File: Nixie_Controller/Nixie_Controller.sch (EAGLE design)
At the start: 59 parts, among them IC1 4028N, T1 MMBTA42, T10 MMBTA42, T11 MMBTA42, T12 MMBTA42, T13 MMBTA42, T14 MMBTA42, T2 MMBTA42, T3 MMBTA42, T4 MMBTA42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

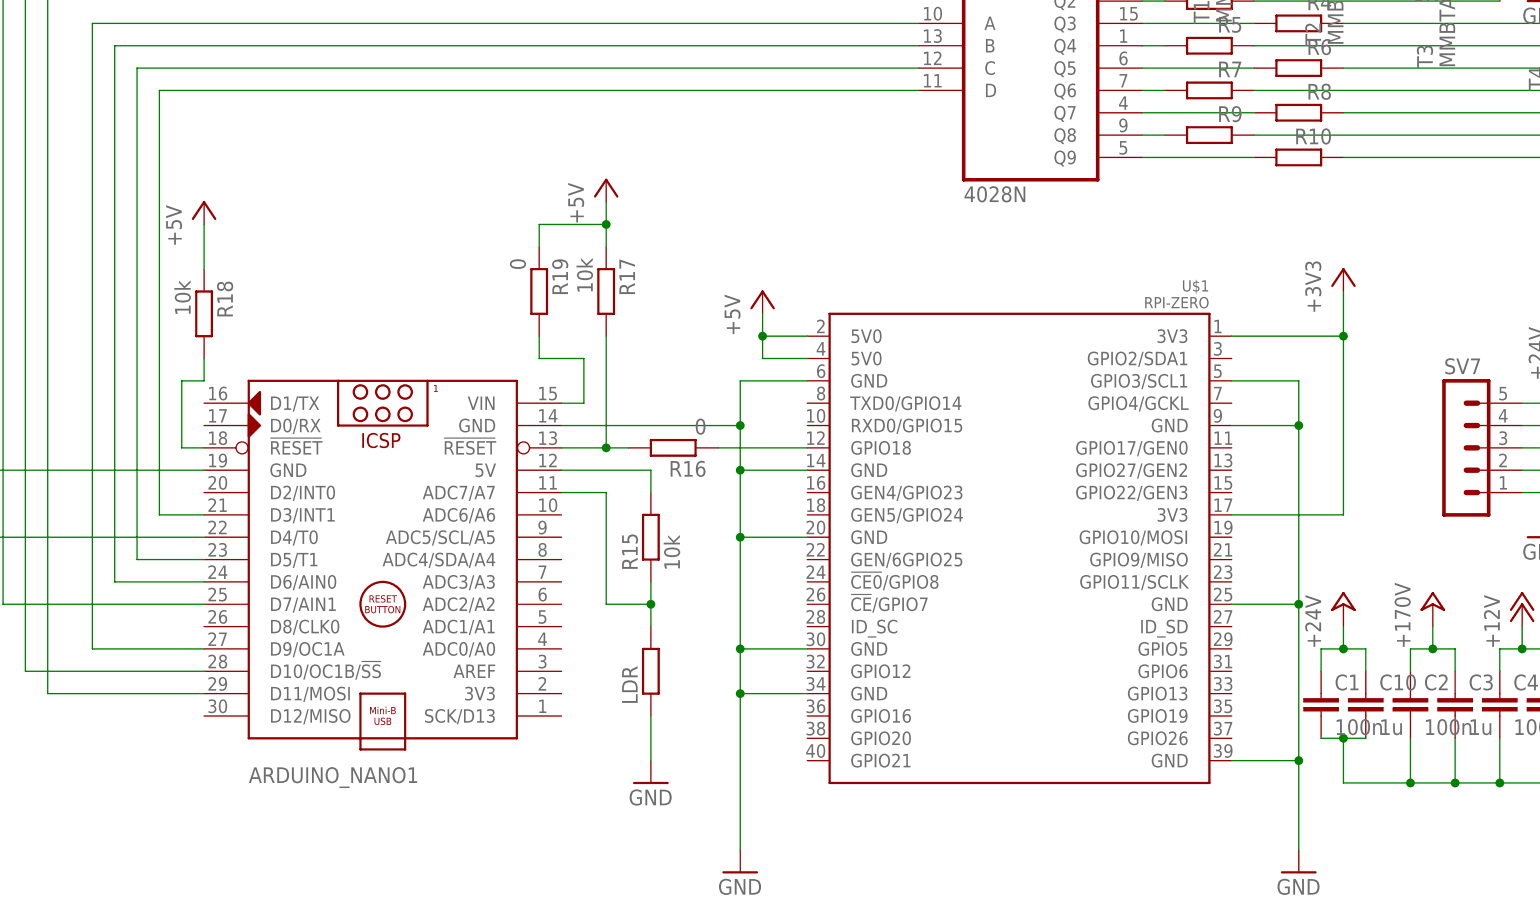
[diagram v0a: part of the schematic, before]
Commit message: fix: add zero ohms to supplies
Add a zero ohm resistor between the Arduino 3.3V and the 3.3V supply voltage.
Add a zero ohm resistor between the raspberry pi 5V and 3.3V and their respective supply voltages.
Remove the second connection to the arduino reset, because they are internally connected
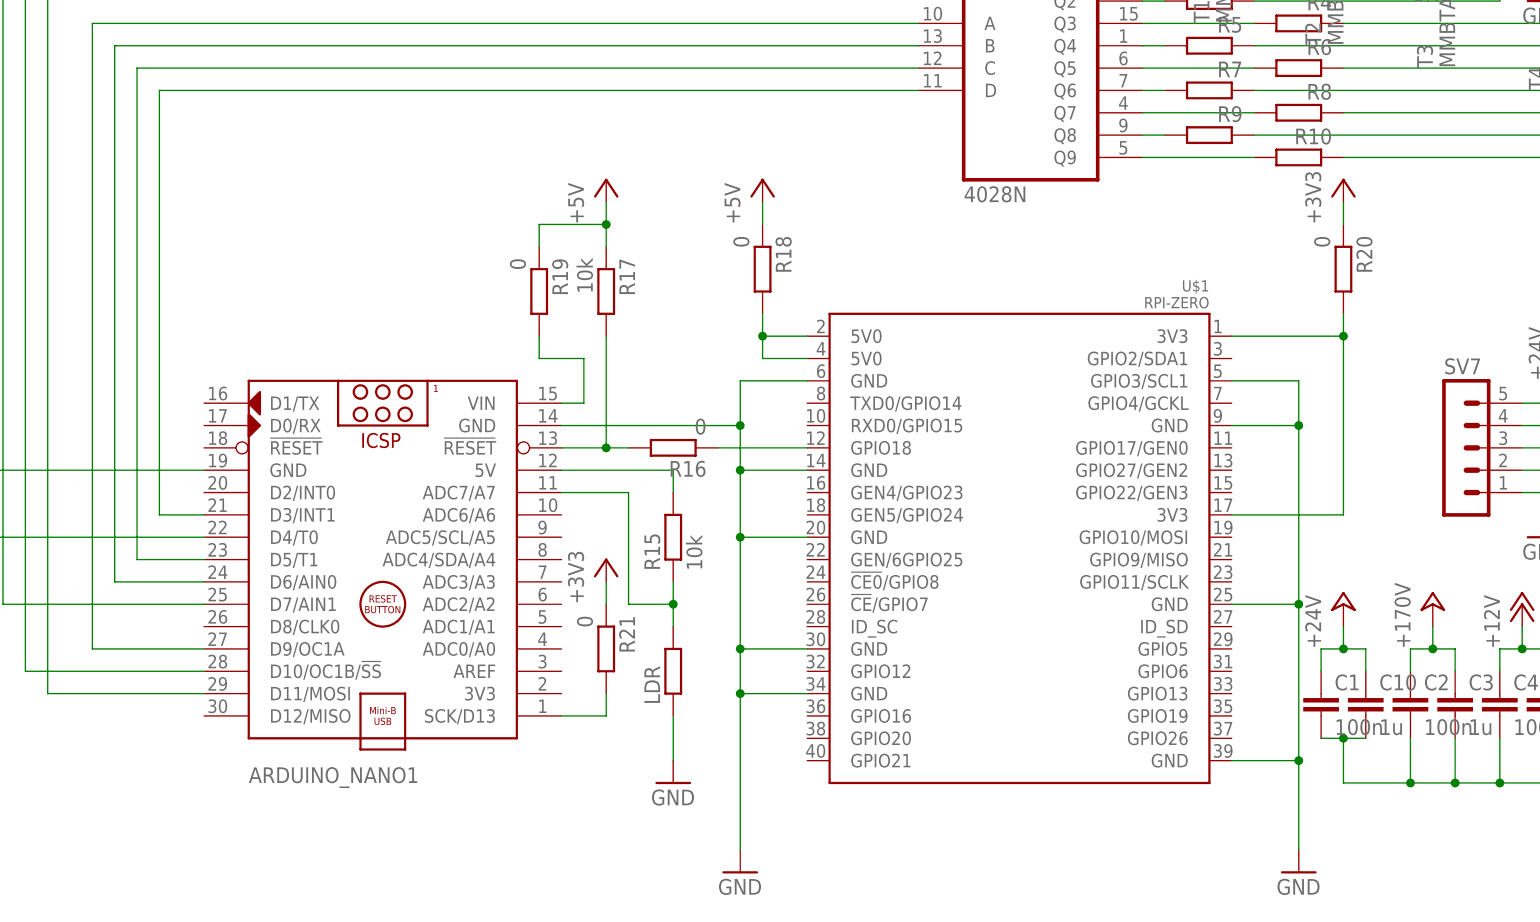
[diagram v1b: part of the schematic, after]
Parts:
- added R20, R21: 0, resistor:R-EU_R0603
- R18: value 10k -> 0
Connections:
- removed net N$95: ARDUINO_NANO1.!RESET@1, R18.2
- new net 3V3@2: R20.2, U$1.3V3@1, U$1.3V3@2
- new net N$39: ARDUINO_NANO1.SCK/D13, R21.2
- net +3V3: now also R20.1, R21.1; no longer U$1.3V3@1, U$1.3V3@2
- net VDD: now also R18.2
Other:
- moved on the sheet: LDR, R15, R18
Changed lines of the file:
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@@
 <part name="R16" library="resistor" deviceset="R-EU_" device="R0603" value="0"/>
 <part name="R17" library="resistor" deviceset="R-EU_" device="R0603" value="10k"/>
-<part name="R18" library="resistor" deviceset="R-EU_" device="R0603" value="10k"/>
-<part name="P+17" library="supply1" deviceset="+5V" device=""/>
 <part name="P+18" library="supply1" deviceset="+5V" device=""/>
 <part name="R19" library="resistor" deviceset="R-EU_" device="R0603" value="0"/>
 <part name="GND19" library="supply1" deviceset="GND" device=""/>
 <part name="GND20" library="supply1" deviceset="GND" device=""/>
+<part name="+3V5" library="supply1" deviceset="+3V3" device=""/>
+<part name="R18" library="resistor" deviceset="R-EU_" device="R0603" value="0"/>
+<part name="R20" library="resistor" deviceset="R-EU_" device="R0603" value="0"/>
+<part name="R21" library="resistor" deviceset="R-EU_" device="R0603" value="0"/>
 </parts>
 <sheets>
@@
 <instance part="SV4" gate="1" x="180.34" y="292.1" rot="MR0"/>
 <instance part="SV2" gate="1" x="180.34" y="236.22" rot="MR0"/>
-<instance part="+3V1" gate="G$1" x="109.22" y="170.18"/>
+<instance part="+3V1" gate="G$1" x="109.22" y="180.34"/>
 <instance part="P+8" gate="1" x="243.84" y="160.02"/>
 <instance part="GND44" gate="1" x="104.14" y="101.6"/>
@@
 <instance part="R12" gate="G$1" x="215.9" y="332.74" rot="R90"/>
 <instance part="R11" gate="G$1" x="223.52" y="320.04" rot="R90"/>
-<instance part="LDR" gate="G$1" x="30.48" y="124.46" rot="R90"/>
-<instance part="R15" gate="G$1" x="30.48" y="139.7" rot="R90"/>
+<instance part="LDR" gate="G$1" x="33.02" y="124.46" rot="R90"/>
+<instance part="R15" gate="G$1" x="33.02" y="139.7" rot="R90"/>
 <instance part="T1" gate="G$1" x="101.6" y="208.28" rot="R90"/>
 <instance part="T2" gate="G$1" x="114.3" y="205.74" rot="R90"/>
@@
 <instance part="ARDUINO_NANO1" gate="G$1" x="0" y="132.08"/>
 <instance part="GND16" gate="1" x="-48.26" y="111.76"/>
-<instance part="GND17" gate="1" x="30.48" y="111.76"/>
-<instance part="P+7" gate="1" x="43.18" y="167.64"/>
+<instance part="GND17" gate="1" x="33.02" y="111.76"/>
+<instance part="P+7" gate="1" x="43.18" y="180.34"/>
 <instance part="U$1" gate="G$1" x="73.66" y="132.08" rot="MR0"/>
 <instance part="SV6" gate="G$1" x="165.1" y="147.32"/>
@@
 <instance part="R16" gate="G$1" x="33.02" y="149.86" rot="R180"/>
 <instance part="R17" gate="G$1" x="25.4" y="167.64" rot="R270"/>
-<instance part="R18" gate="G$1" x="-20.32" y="165.1" rot="R270"/>
-<instance part="P+17" gate="1" x="-20.32" y="177.8"/>
 <instance part="P+18" gate="1" x="25.4" y="180.34"/>
 <instance part="R19" gate="G$1" x="17.78" y="167.64" rot="R270"/>
 <instance part="GND19" gate="1" x="317.5" y="200.66"/>
 <instance part="GND20" gate="1" x="317.5" y="109.22"/>
+<instance part="+3V5" gate="G$1" x="25.4" y="137.16"/>
+<instance part="R18" gate="G$1" x="43.18" y="170.18" rot="R270"/>
+<instance part="R20" gate="G$1" x="109.22" y="170.18" rot="R270"/>
+<instance part="R21" gate="G$1" x="25.4" y="127" rot="R270"/>
 </instances>
 <busses>
@@
 <pinref part="LDR" gate="G$1" pin="1"/>
 <pinref part="GND17" gate="1" pin="GND"/>
-<wire x1="30.48" y1="114.3" x2="30.48" y2="119.38" width="0.1524" layer="91"/>
+<wire x1="33.02" y1="114.3" x2="33.02" y2="119.38" width="0.1524" layer="91"/>
 </segment>
 <segment>
@@
 <net name="+3V3" class="0">
 <segment>
-<pinref part="+3V1" gate="G$1" pin="+3V3"/>
-<wire x1="109.22" y1="167.64" x2="109.22" y2="162.56" width="0.1524" layer="91"/>
-<wire x1="109.22" y1="162.56" x2="109.22" y2="142.24" width="0.1524" layer="91"/>
-<wire x1="96.52" y1="162.56" x2="109.22" y2="162.56" width="0.1524" layer="91"/>
-<junction x="109.22" y="162.56"/>
-<wire x1="109.22" y1="142.24" x2="96.52" y2="142.24" width="0.1524" layer="91"/>
-<pinref part="U$1" gate="G$1" pin="3V3@1"/>
-<pinref part="U$1" gate="G$1" pin="3V3@2"/>
-</segment>
-<segment>
 <pinref part="SV7" gate="G$1" pin="2"/>
 <pinref part="+3V2" gate="G$1" pin="+3V3"/>
@@
 <wire x1="172.72" y1="144.78" x2="200.66" y2="144.78" width="0.1524" layer="91"/>
 <wire x1="200.66" y1="144.78" x2="200.66" y2="157.48" width="0.1524" layer="91"/>
+</segment>
+<segment>
+<pinref part="+3V5" gate="G$1" pin="+3V3"/>
+<pinref part="R21" gate="G$1" pin="1"/>
+<wire x1="25.4" y1="134.62" x2="25.4" y2="132.08" width="0.1524" layer="91"/>
+</segment>
+<segment>
+<pinref part="+3V1" gate="G$1" pin="+3V3"/>
+<pinref part="R20" gate="G$1" pin="1"/>
+<wire x1="109.22" y1="177.8" x2="109.22" y2="175.26" width="0.1524" layer="91"/>
 </segment>
 </net>
@@
 </segment>
 <segment>
-<pinref part="P+7" gate="1" pin="+5V"/>
 <wire x1="48.26" y1="160.02" x2="43.18" y2="160.02" width="0.1524" layer="91"/>
 <wire x1="43.18" y1="160.02" x2="43.18" y2="162.56" width="0.1524" layer="91"/>
-<wire x1="43.18" y1="165.1" x2="43.18" y2="162.56" width="0.1524" layer="91"/>
 <wire x1="43.18" y1="162.56" x2="48.26" y2="162.56" width="0.1524" layer="91"/>
-<junction x="43.18" y="162.56"/>
 <pinref part="U$1" gate="G$1" pin="5V0@1"/>
 <pinref part="U$1" gate="G$1" pin="5V0@2"/>
+<pinref part="R18" gate="G$1" pin="2"/>
+<wire x1="43.18" y1="165.1" x2="43.18" y2="162.56" width="0.1524" layer="91"/>
+<junction x="43.18" y="162.56"/>
 </segment>
 <segment>
@@
 <pinref part="ARDUINO_NANO1" gate="G$1" pin="5V"/>
 <pinref part="R15" gate="G$1" pin="2"/>
-<wire x1="20.32" y1="147.32" x2="30.48" y2="147.32" width="0.1524" layer="91"/>
-<wire x1="30.48" y1="147.32" x2="30.48" y2="144.78" width="0.1524" layer="91"/>
+<wire x1="20.32" y1="147.32" x2="33.02" y2="147.32" width="0.1524" layer="91"/>
+<wire x1="33.02" y1="147.32" x2="33.02" y2="144.78" width="0.1524" layer="91"/>
 </segment>
 </net>
@@
 <pinref part="R15" gate="G$1" pin="1"/>
 <pinref part="LDR" gate="G$1" pin="2"/>
-<wire x1="30.48" y1="134.62" x2="30.48" y2="132.08" width="0.1524" layer="91"/>
-<wire x1="30.48" y1="132.08" x2="30.48" y2="129.54" width="0.1524" layer="91"/>
-<wire x1="30.48" y1="132.08" x2="25.4" y2="132.08" width="0.1524" layer="91"/>
-<wire x1="25.4" y1="132.08" x2="25.4" y2="144.78" width="0.1524" layer="91"/>
+<wire x1="33.02" y1="134.62" x2="33.02" y2="132.08" width="0.1524" layer="91"/>
+<wire x1="33.02" y1="132.08" x2="33.02" y2="129.54" width="0.1524" layer="91"/>
+<wire x1="33.02" y1="132.08" x2="27.94" y2="132.08" width="0.1524" layer="91"/>
+<wire x1="27.94" y1="132.08" x2="27.94" y2="144.78" width="0.1524" layer="91"/>
 <pinref part="ARDUINO_NANO1" gate="G$1" pin="ADC7/A7"/>
-<wire x1="25.4" y1="144.78" x2="20.32" y2="144.78" width="0.1524" layer="91"/>
-<junction x="30.48" y="132.08"/>
+<wire x1="27.94" y1="144.78" x2="20.32" y2="144.78" width="0.1524" layer="91"/>
+<junction x="33.02" y="132.08"/>
 </segment>
 </net>
@@
 </segment>
 </net>
-<net name="N$95" class="0">
-<segment>
-<pinref part="ARDUINO_NANO1" gate="G$1" pin="!RESET@1"/>
-<wire x1="-20.32" y1="149.86" x2="-22.86" y2="149.86" width="0.1524" layer="91"/>
-<wire x1="-22.86" y1="149.86" x2="-22.86" y2="157.48" width="0.1524" layer="91"/>
-<wire x1="-22.86" y1="157.48" x2="-20.32" y2="157.48" width="0.1524" layer="91"/>
-<pinref part="R18" gate="G$1" pin="2"/>
-<wire x1="-20.32" y1="157.48" x2="-20.32" y2="160.02" width="0.1524" layer="91"/>
-</segment>
-</net>
 <net name="+5V" class="0">
 <segment>
@@
 </segment>
 <segment>
+<pinref part="P+7" gate="1" pin="+5V"/>
 <pinref part="R18" gate="G$1" pin="1"/>
-<pinref part="P+17" gate="1" pin="+5V"/>
-<wire x1="-20.32" y1="175.26" x2="-20.32" y2="170.18" width="0.1524" layer="91"/>
+<wire x1="43.18" y1="177.8" x2="43.18" y2="175.26" width="0.1524" layer="91"/>
 </segment>
 </net>
@@
 </segment>
 </net>
+<net name="N$39" class="0">
+<segment>
+<pinref part="ARDUINO_NANO1" gate="G$1" pin="SCK/D13"/>
+<pinref part="R21" gate="G$1" pin="2"/>
+<wire x1="20.32" y1="119.38" x2="25.4" y2="119.38" width="0.1524" layer="91"/>
+<wire x1="25.4" y1="119.38" x2="25.4" y2="121.92" width="0.1524" layer="91"/>
+</segment>
+</net>
+<net name="3V3@2" class="0">
+<segment>
+<wire x1="109.22" y1="162.56" x2="109.22" y2="142.24" width="0.1524" layer="91"/>
+<wire x1="96.52" y1="162.56" x2="109.22" y2="162.56" width="0.1524" layer="91"/>
+<wire x1="109.22" y1="142.24" x2="96.52" y2="142.24" width="0.1524" layer="91"/>
+<pinref part="U$1" gate="G$1" pin="3V3@1"/>
+<pinref part="U$1" gate="G$1" pin="3V3@2"/>
+<pinref part="R20" gate="G$1" pin="2"/>
+<wire x1="109.22" y1="162.56" x2="109.22" y2="165.1" width="0.1524" layer="91"/>
+<junction x="109.22" y="162.56"/>
+</segment>
+</net>

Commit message: fix: add resistors from schematic fix
Add the three 0 ohm resistors to the board, which were added in the schematic fix
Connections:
- net +5V: now also R18.2, U$1.5V0@1, U$1.5V0@2; no longer R17.1, R18.1, R19.1
- net VDD: now also R17.1, R18.1, R19.1; no longer R18.2, U$1.5V0@1, U$1.5V0@2
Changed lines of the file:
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@@
-</segment>
-<segment>
-<wire x1="48.26" y1="160.02" x2="43.18" y2="160.02" width="0.1524" layer="91"/>
-<wire x1="43.18" y1="160.02" x2="43.18" y2="162.56" width="0.1524" layer="91"/>
-<wire x1="43.18" y1="162.56" x2="48.26" y2="162.56" width="0.1524" layer="91"/>
-<pinref part="U$1" gate="G$1" pin="5V0@1"/>
-<pinref part="U$1" gate="G$1" pin="5V0@2"/>
-<pinref part="R18" gate="G$1" pin="2"/>
-<wire x1="43.18" y1="165.1" x2="43.18" y2="162.56" width="0.1524" layer="91"/>
-<junction x="43.18" y="162.56"/>
 </segment>
 <segment>
@@
 <wire x1="236.22" y1="208.28" x2="238.76" y2="208.28" width="0.1524" layer="91"/>
 <wire x1="238.76" y1="208.28" x2="238.76" y2="220.98" width="0.1524" layer="91"/>
+</segment>
+<segment>
+<pinref part="R17" gate="G$1" pin="1"/>
+<pinref part="P+18" gate="1" pin="+5V"/>
+<wire x1="25.4" y1="177.8" x2="25.4" y2="175.26" width="0.1524" layer="91"/>
+<pinref part="R19" gate="G$1" pin="1"/>
+<wire x1="25.4" y1="175.26" x2="25.4" y2="172.72" width="0.1524" layer="91"/>
+<wire x1="17.78" y1="172.72" x2="17.78" y2="175.26" width="0.1524" layer="91"/>
+<wire x1="17.78" y1="175.26" x2="25.4" y2="175.26" width="0.1524" layer="91"/>
+<junction x="25.4" y="175.26"/>
+</segment>
+<segment>
+<pinref part="P+7" gate="1" pin="+5V"/>
+<pinref part="R18" gate="G$1" pin="1"/>
+<wire x1="43.18" y1="177.8" x2="43.18" y2="175.26" width="0.1524" layer="91"/>
 </segment>
 </net>
@@
 </segment>
 </net>
-<net name="+5V" class="0">
-<segment>
-<pinref part="R17" gate="G$1" pin="1"/>
-<pinref part="P+18" gate="1" pin="+5V"/>
-<wire x1="25.4" y1="177.8" x2="25.4" y2="175.26" width="0.1524" layer="91"/>
-<pinref part="R19" gate="G$1" pin="1"/>
-<wire x1="25.4" y1="175.26" x2="25.4" y2="172.72" width="0.1524" layer="91"/>
-<wire x1="17.78" y1="172.72" x2="17.78" y2="175.26" width="0.1524" layer="91"/>
-<wire x1="17.78" y1="175.26" x2="25.4" y2="175.26" width="0.1524" layer="91"/>
-<junction x="25.4" y="175.26"/>
-</segment>
-<segment>
-<pinref part="P+7" gate="1" pin="+5V"/>
-<pinref part="R18" gate="G$1" pin="1"/>
-<wire x1="43.18" y1="177.8" x2="43.18" y2="175.26" width="0.1524" layer="91"/>
-</segment>
-</net>
 <net name="N$96" class="0">
 <segment>
@@
 </segment>
 </net>
+<net name="+5V" class="0">
+<segment>
+<wire x1="48.26" y1="160.02" x2="43.18" y2="160.02" width="0.1524" layer="91"/>
+<wire x1="43.18" y1="160.02" x2="43.18" y2="162.56" width="0.1524" layer="91"/>
+<wire x1="43.18" y1="162.56" x2="48.26" y2="162.56" width="0.1524" layer="91"/>
+<pinref part="U$1" gate="G$1" pin="5V0@1"/>
+<pinref part="U$1" gate="G$1" pin="5V0@2"/>
+<pinref part="R18" gate="G$1" pin="2"/>
+<wire x1="43.18" y1="165.1" x2="43.18" y2="162.56" width="0.1524" layer="91"/>
+<junction x="43.18" y="162.56"/>
+</segment>
+</net>

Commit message: feat: Add double anode nixie support
Add support for nixie tubes that use two anodes.
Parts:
- added R22, R23, R24, R25: 22k, resistor:R-EU_R0603
- added T15, T16, T17, T18: MMBTA42, transistor:BC850
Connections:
- new net N$101: ARDUINO_NANO1.SCK/D13, T15.B
- new net N$102: ARDUINO_NANO1.D2/INT0, T18.B
- new net N$103: ARDUINO_NANO1.D8/CLK0, T17.B
- new net N$104: ARDUINO_NANO1.D12/MISO, T16.B
- new net N$57: R22.1, T15.C
- new net N$58: R25.1, T18.C
- new net N$69: R24.1, T17.C
- new net N$70: R23.1, T16.C
- new net N$76: SV4.12, T15.E
- new net N$82: SV3.12, T16.E
- new net N$88: SV2.12, T17.E
- new net N$95: SV1.12, T18.E
- net +170V: now also R22.2, R23.2, R24.2, R25.2
- net N$39: now also ARDUINO_NANO1.3V3; no longer ARDUINO_NANO1.SCK/D13
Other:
- moved on the sheet: ARDUINO_NANO1, LDR, R15, R16, R17, R19, R21, SV10, SV8, SV9

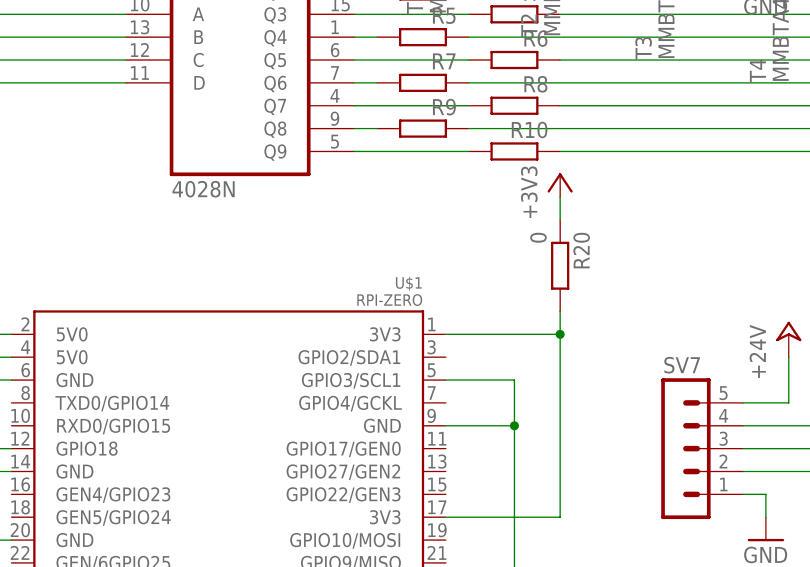
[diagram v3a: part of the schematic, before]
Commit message: fix: Change names
Change the names of the Raspberry Pi and the USB-C connectors to something more meaningfull.
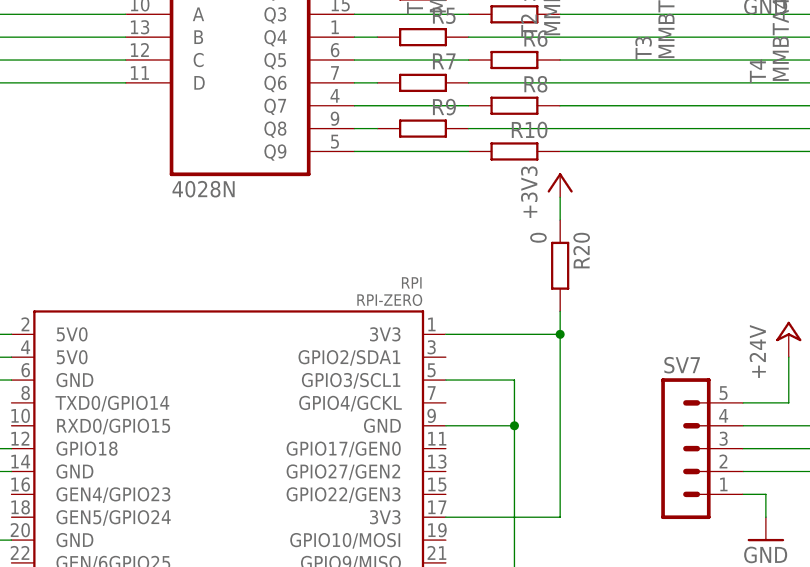
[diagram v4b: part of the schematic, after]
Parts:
- renumbered U$1 to RPI, U$2 to USBC2, U$3 to USBC1
